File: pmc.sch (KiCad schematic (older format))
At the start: 165 parts, among them M1 TPS61040, M2 LM46001, M3 STM32F405RG, M4 REF3033, M5 TPS73633, M6 SN65HVD233, M7 UCC27211A, M8 UCC27211A, M9 UCC27211A, P1 FAN, P10 F1, P11 F2, P12 A1, P13 A2, P14 BOOT, P15 F1, P16 F2, P17 A1, P18 A2, P19 CONN4, P2 NTC, P20 CONN4, P21 CONN4, P22 CONN4, P23 CONN4, P3 HALL, P4 SPI, P5 PPM, P6 ANALOG, P7 CAN, P8 SWD, P9 USART, Q1 IRLML6401, Q2 IPT007N06N, Q3 IPT007N06N, Q4 IPT007N06N, Q5 IPT007N06N, Q6 IPT007N06N, Q7 IPT007N06N, U1 AD8539, U2 AD8539, U3 AD8417, U4 AD8417

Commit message: Moved CAN to 5v, fixed filter capacitors, etc.
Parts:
- removed M6: SN65HVD233, foot:SO-8, symbol SN65HVD23X
- removed R45, R46: 1K 1%, foot:SM-0603, symbol R
- added C66: 100nF 25v, foot:SM-0603, symbol C
- added M6: SN65HVD256, foot:SO-8, symbol SN65HVD256
- C41, C42, C43, C44: value 47pF C0G -> 1nF C0G
- R8: value 11.3K 1% -> 13.7K 1%
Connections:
- net +3.3V: now also C66.1, M6.5 (VRXD); no longer C35.2, C36.2
- net +5V: now also C35.2, C36.2, M6.3 (VCC)
- net AGND: now also C66.2, M6.2 (GND), M6.8 (S)
- net CAN_RX: now also M6.4 (RXD)
- net CAN_TX: now also M6.1 (TXD)
- net CURRENT_A: now also P17.3
- net CURRENT_B: now also P17.4
- net at P7.2, R35.1, R51.1: now also M6.6 (CANL)
- net at P7.1, R35.2, R51.2: now also M6.7 (CANH)
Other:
- note added: "Pulse control inputs:\n * RC servo pulse width\n * STEP/DIR\n * QEP\nor I2C bus or Data-USART"
- note added: "R33 is not fitted\n"
- note added: "Vfb = 1.016v"
- note added: "Vfb = 1.233v"
- note removed: "Balance resistors R45-R46 are needed only in case of parallel\nconnection of multiple power boards\n"
- note removed: "Pulse control inputs:\n * RC servo PPM\n * STEP/DIR\n * QEP\nor I2C bus or USART"
- note removed: "R33 is not fitted if 3.3vREF voltage reference is used\n"
- moved on the sheet: R35, R51
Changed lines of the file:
@@
 Sheet 1 1
 Title "Phobia Motor Controller"
-Date "2018-12-10"
+Date "2019-03-23"
 Rev "4c"
 Comp "Roman Belov"
@@
 P 5450 5250
 F 0 "R8" V 5550 5050 60  0000 C CNN
-F 1 "11.3K 1%" V 5400 4900 60  0000 C CNN
+F 1 "13.7K 1%" V 5400 4900 60  0000 C CNN
 F 2 "foot:SM-0603" H 5450 5250 60  0001 C CNN
 F 3 "" H 5450 5250 60  0000 C CNN
@@
 U 1 1 59D934A0
 P 13250 2050
-F 0 "C41" V 13350 1850 60  0000 C CNN
-F 1 "47pF C0G" V 13150 1700 60  0000 C CNN
+F 0 "C41" V 13300 1800 60  0000 C CNN
+F 1 "1nF C0G" V 13150 1700 60  0000 C CNN
 F 2 "foot:SM-0603" H 13250 2050 60  0001 C CNN
 F 3 "" H 13250 2050 60  0000 C CNN
@@
 	0    -1   -1   0
 $EndComp
-$Comp
-L SN65HVD23X M6
-U 1 1 59D934A6
-P 10050 13250
-F 0 "M6" H 10050 13600 60  0000 C CNN
-F 1 "SN65HVD233" H 10000 12900 60  0000 C CNN
-F 2 "foot:SO-8" H 9600 12900 60  0001 C CNN
-F 3 "" H 10050 13250 60  0000 C CNN
-	1    10050 13250
-	1    0    0    -1
-$EndComp
 Text GLabel 6850 9750 2    60   Input ~ 0
 CAN_RX
@@
 L +3.3V #PWR021
 U 1 1 59D934A7
-P 8900 14200
-F 0 "#PWR021" H 8900 14290 20  0001 C CNN
-F 1 "+3.3V" V 8900 14550 60  0000 C CNN
-F 2 "" H 8900 14200 60  0000 C CNN
-F 3 "" H 8900 14200 60  0000 C CNN
-	1    8900 14200
+P 10250 13750
+F 0 "#PWR021" H 10250 13840 20  0001 C CNN
+F 1 "+3.3V" V 10250 14100 60  0000 C CNN
+F 2 "" H 10250 13750 60  0000 C CNN
+F 3 "" H 10250 13750 60  0000 C CNN
+	1    10250 13750
 	0    -1   -1   0
 $EndComp
@@
 L R R35
 U 1 1 59D934AA
-P 11350 13400
-F 0 "R35" H 11750 13400 60  0000 C CNN
-F 1 "820" H 11000 13400 60  0000 C CNN
-F 2 "foot:SM-1206" H 11350 13400 60  0001 C CNN
-F 3 "" H 11350 13400 60  0000 C CNN
-	1    11350 13400
+P 11600 13400
+F 0 "R35" H 12000 13400 60  0000 C CNN
+F 1 "820" H 11250 13400 60  0000 C CNN
+F 2 "foot:SM-1206" H 11600 13400 60  0001 C CNN
+F 3 "" H 11600 13400 60  0000 C CNN
+	1    11600 13400
 	-1   0    0    1
 $EndComp
@@
 U 1 1 59D934AB
 P 9350 13750
-F 0 "C35" H 9000 13850 60  0000 C CNN
-F 1 "100nF 25v" H 9850 13650 60  0000 C CNN
+F 0 "C35" H 8950 13800 60  0000 C CNN
+F 1 "100nF 25v" H 8850 13650 60  0000 C CNN
 F 2 "foot:SM-0603" H 9350 13750 60  0001 C CNN
 F 3 "" H 9350 13750 60  0000 C CNN
@@
 U 1 1 59D934AC
 P 9350 14200
-F 0 "C36" H 9365 14030 60  0000 C CNN
-F 1 "1uF 25v" H 9800 14100 60  0000 C CNN
+F 0 "C36" H 9150 14050 60  0000 C CNN
+F 1 "1uF 25v" H 9200 13900 60  0000 C CNN
 F 2 "foot:SM-0805" H 9350 14200 60  0001 C CNN
 F 3 "" H 9350 14200 60  0000 C CNN
@@
 L GND #PWR023
 U 1 1 59D934AD
-P 10600 13850
-F 0 "#PWR023" H 10600 13850 30  0001 C CNN
-F 1 "GND" H 10600 13780 30  0001 C CNN
-F 2 "" H 10600 13850 60  0000 C CNN
-F 3 "" H 10600 13850 60  0000 C CNN
-	1    10600 13850
+P 10900 14150
+F 0 "#PWR023" H 10900 14150 30  0001 C CNN
+F 1 "GND" H 10900 14080 30  0001 C CNN
+F 2 "" H 10900 14150 60  0000 C CNN
+F 3 "" H 10900 14150 60  0000 C CNN
+	1    10900 14150
 	1    0    0    -1
 $EndComp
@@
 U 1 1 59D934C4
 P 13250 3400
-F 0 "C42" V 13350 3200 60  0000 C CNN
-F 1 "47pF C0G" V 13150 3050 60  0000 C CNN
+F 0 "C42" V 13300 3150 60  0000 C CNN
+F 1 "1nF C0G" V 13150 3050 60  0000 C CNN
 F 2 "foot:SM-0603" H 13250 3400 60  0001 C CNN
 F 3 "" H 13250 3400 60  0000 C CNN
@@
 U 1 1 59F72F54
 P 13250 4750
-F 0 "C43" V 13350 4550 60  0000 C CNN
-F 1 "47pF C0G" V 13150 4400 60  0000 C CNN
+F 0 "C43" V 13300 4500 60  0000 C CNN
+F 1 "1nF C0G" V 13150 4400 60  0000 C CNN
 F 2 "foot:SM-0603" H 13250 4750 60  0001 C CNN
 F 3 "" H 13250 4750 60  0000 C CNN
@@
 U 1 1 59F72F7F
 P 13250 6100
-F 0 "C44" V 13350 5900 60  0000 C CNN
-F 1 "47pF C0G" V 13150 5750 60  0000 C CNN
+F 0 "C44" V 13300 5850 60  0000 C CNN
+F 1 "1nF C0G" V 13150 5750 60  0000 C CNN
 F 2 "foot:SM-0603" H 13250 6100 60  0001 C CNN
 F 3 "" H 13250 6100 60  0000 C CNN
@@
 External peripheral SPI device\nor ADC/DAC or GPIO
 Text Notes 12600 10600 0    60   ~ 0
-Pulse control inputs:\n * RC servo PPM\n * STEP/DIR\n * QEP\nor I2C bus or USART
+Pulse control inputs:\n * RC servo pulse width\n * STEP/DIR\n * QEP\nor I2C bus or Data-USART
 Text Notes 15100 14150 0    60   ~ 0
 Flash STM32 microcontroller\nDebug via SWD\nConfigure and control via USART\n
@@
 ADC_IN11
 $Comp
-L R R46
-U 1 1 5B00BFA8
-P 18850 10400
-F 0 "R46" H 19050 10550 60  0000 C CNN
-F 1 "1K 1%" H 18750 10550 60  0000 C CNN
-F 2 "foot:SM-0603" H 18850 10400 60  0001 C CNN
-F 3 "" H 18850 10400 60  0000 C CNN
-	1    18850 10400
-	1    0    0    -1
-$EndComp
-$Comp
-L R R45
-U 1 1 5B0107B7
-P 18350 10500
-F 0 "R45" H 18550 10350 60  0000 C CNN
-F 1 "1K 1%" H 18250 10350 60  0000 C CNN
-F 2 "foot:SM-0603" H 18350 10500 60  0001 C CNN
-F 3 "" H 18350 10500 60  0000 C CNN
-	1    18350 10500
-	1    0    0    -1
-$EndComp
-$Comp
 L R R33
 U 1 1 5B5F338A
@@
 	0    -1   -1   0
 $EndComp
-Text Notes 10700 12900 0    60   ~ 12
+Text Notes 11150 13900 0    60   ~ 12
 Optional termination resistors
 $Comp
@@
 L R R51
 U 1 1 5C351474
-P 11350 13600
-F 0 "R51" H 11750 13600 60  0000 C CNN
-F 1 "820" H 11000 13600 60  0000 C CNN
-F 2 "foot:SM-1206" H 11350 13600 60  0001 C CNN
-F 3 "" H 11350 13600 60  0000 C CNN
-	1    11350 13600
+P 11600 13600
+F 0 "R51" H 12000 13600 60  0000 C CNN
+F 1 "820" H 11250 13600 60  0000 C CNN
+F 2 "foot:SM-1206" H 11600 13600 60  0001 C CNN
+F 3 "" H 11600 13600 60  0000 C CNN
+	1    11600 13600
+	-1   0    0    1
+$EndComp
+Text Notes 18650 12650 0    60   ~ 12
+Current sensing range\n\nRange (A)   Shunt (mOhm)\n-----------------\n      50       0.5\n      80       0.3\n     100      0.25
+Text Notes 10500 3550 0    60   ~ 12
+R33 is not fitted\n
+Text Notes 5550 1750 0    60   ~ 12
+Vfb = 1.016v
+Text Notes 5100 4450 0    60   ~ 12
+Vfb = 1.233v
+$Comp
+L +5V #PWR0107
+U 1 1 5C89DA1F
+P 8900 14200
+F 0 "#PWR0107" H 8900 14290 20  0001 C CNN
+F 1 "+5V" V 8900 14500 60  0000 C CNN
+F 2 "" H 8900 14200 60  0000 C CNN
+F 3 "" H 8900 14200 60  0000 C CNN
+	1    8900 14200
+	0    -1   -1   0
+$EndComp
+$Comp
+L SN65HVD256 M6
+U 1 1 5C8A5FB5
+P 10050 13250
+F 0 "M6" H 9800 13600 60  0000 C CNN
+F 1 "SN65HVD256" H 10250 13600 60  0000 C CNN
+F 2 "foot:SO-8" H 9600 12900 60  0001 C CNN
+F 3 "" H 10050 13250 60  0000 C CNN
+	1    10050 13250
+	1    0    0    -1
+$EndComp
+$Comp
+L C C66
+U 1 1 5C8AE35E
+P 10700 13750
+F 0 "C66" H 10900 13900 60  0000 C CNN
+F 1 "100nF 25v" H 10850 14050 60  0000 C CNN
+F 2 "foot:SM-0603" H 10700 13750 60  0001 C CNN
+F 3 "" H 10700 13750 60  0000 C CNN
+	1    10700 13750
 	-1   0    0    1
 $EndComp
@@
 Wire Wire Line
 	6700 11500 6700 11600
-Connection ~ 10600 13400
-Wire Wire Line
-	10500 13400 10600 13400
-Wire Wire Line
-	10600 13300 10500 13300
-Wire Wire Line
-	10600 13300 10600 13850
-Connection ~ 11500 13100
-Connection ~ 11150 13200
+Connection ~ 11750 13100
+Connection ~ 11400 13200
 Wire Wire Line
 	10500 13200 12000 13200
@@
 	16300 10200 16100 10200
 Wire Wire Line
-	17400 10400 18700 10400
-Wire Wire Line
 	18500 11300 17400 11300
 Wire Wire Line
@@
 	15200 10400 16300 10400
 Wire Wire Line
-	19050 10400 19300 10400
-Wire Wire Line
-	17400 10500 18200 10500
-Wire Wire Line
-	18550 10500 18700 10500
-Wire Wire Line
 	18700 10500 18700 10600
 Wire Wire Line
@@
 Connection ~ 8650 4700
 Wire Wire Line
-	11150 13200 11150 13600
-Connection ~ 11150 13400
+	11400 13200 11400 13600
+Connection ~ 11400 13400
 Wire Wire Line
-	11500 13100 11500 13600
-Connection ~ 11500 13400
-Text Notes 18650 12650 0    60   ~ 12
-Current sensing range\n\nRange (A)   Shunt (mOhm)\n-----------------\n      50       0.5\n      80       0.3\n     100      0.25
-Text Notes 18750 10950 0    60   ~ 12
-Balance resistors R45-R46 are needed only in case of parallel\nconnection of multiple power boards\n
-Text Notes 9250 4000 0    60   ~ 12
-R33 is not fitted if 3.3vREF voltage reference is used\n
+	11750 13100 11750 13600
+Connection ~ 11750 13400
+Wire Wire Line
+	10500 13300 10900 13300
+Wire Wire Line
+	10900 13750 10850 13750
+Wire Wire Line
+	10250 13750 10550 13750
+Connection ~ 10500 13750
+Connection ~ 10900 13750
+Wire Wire Line
+	10500 13750 10500 13400
+Wire Wire Line
+	10900 13300 10900 14150
+Wire Wire Line
+	18700 10500 17400 10500
+Wire Wire Line
+	17400 10400 19300 10400
 $EndSCHEMATC

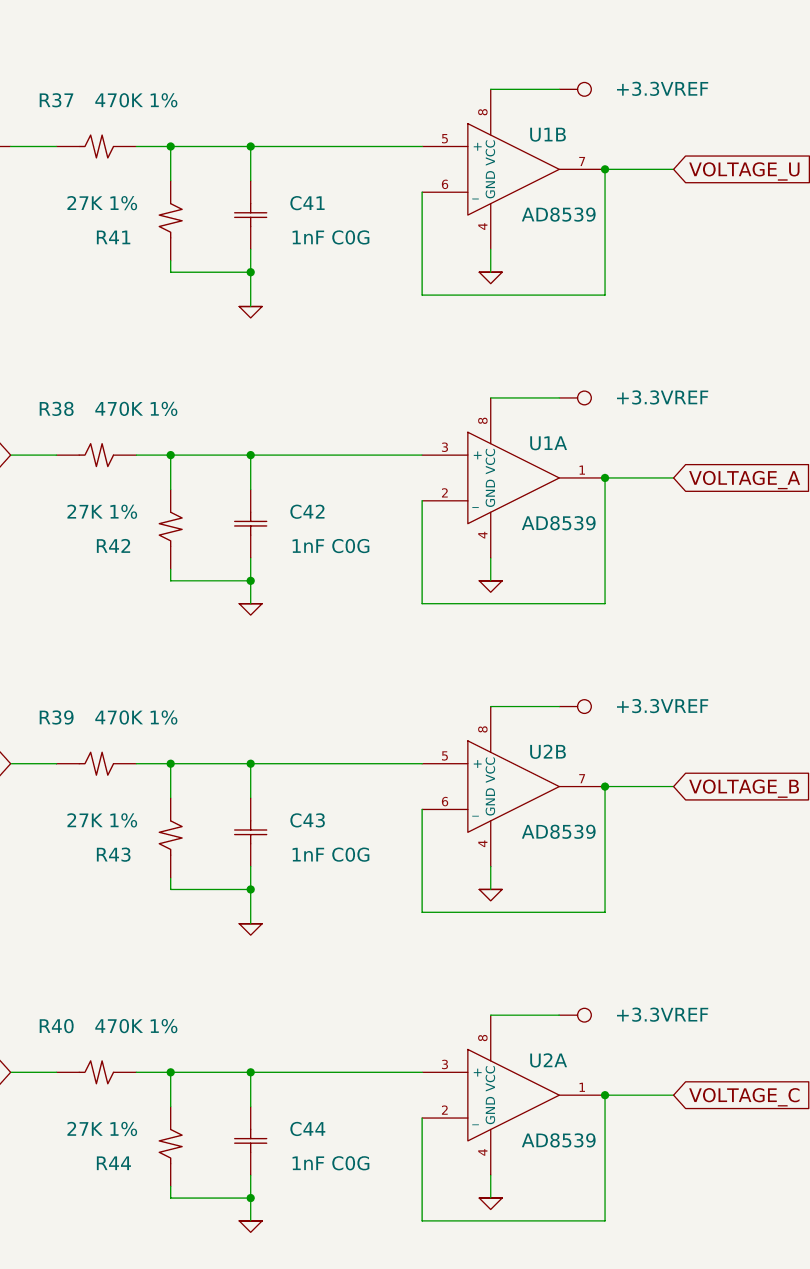
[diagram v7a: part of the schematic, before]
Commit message: Added voltage bias resistors.
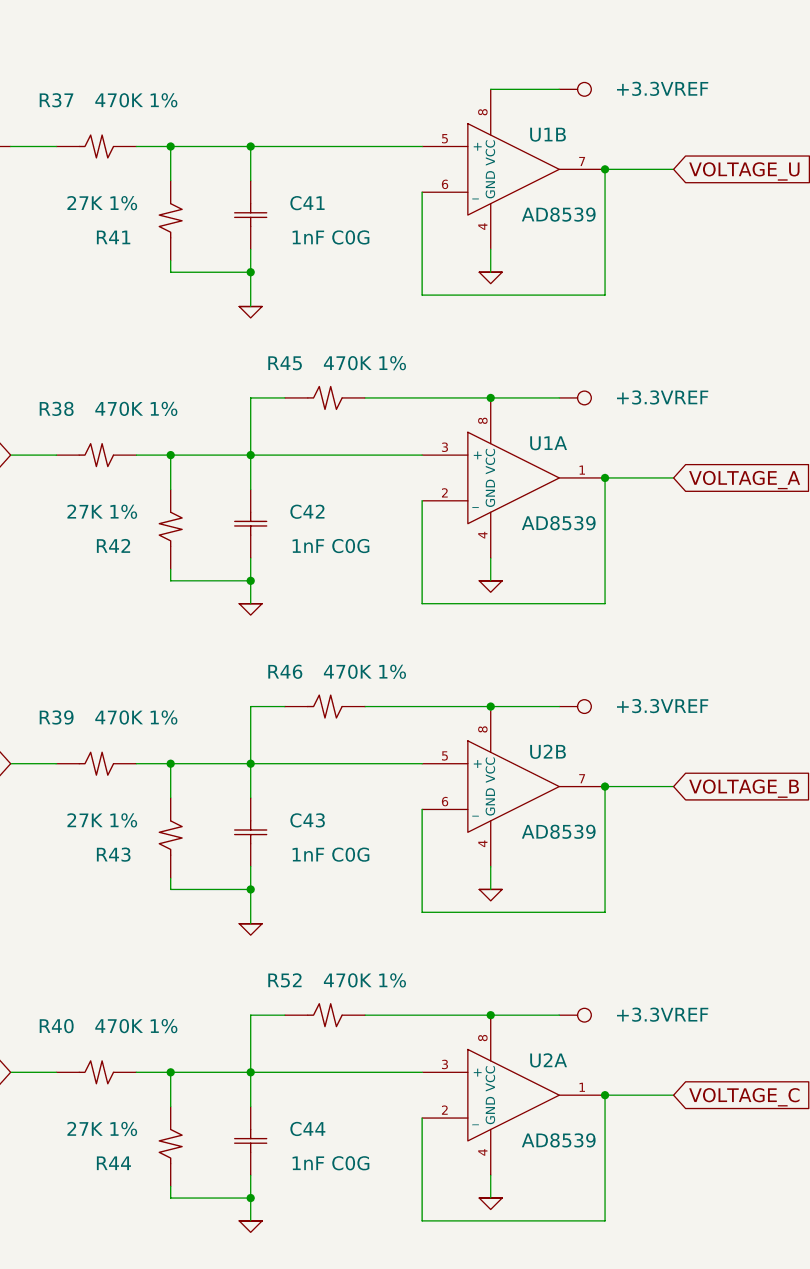
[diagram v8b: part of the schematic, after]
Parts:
- added R45, R46, R52: 470K 1%, foot:SM-0603, symbol R
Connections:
- net +3.3VREF: now also R45.2, R46.2, R52.2
- net at C42.1, R38.2, R42.2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: now also R45.1
- net at C43.1, R39.2, R43.2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: now also R46.1
- net at C44.1, R40.2, R44.2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: now also R52.1
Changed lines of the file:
@@
 Sheet 1 1
 Title "Phobia Motor Controller"
-Date "2019-03-23"
+Date "2019-04-27"
 Rev "4c"
 Comp "Roman Belov"
@@
 	13250 3550 13250 3750
 Wire Wire Line
-	13250 3100 13250 3250
+	13250 2850 13250 3250
 Wire Wire Line
 	13250 2200 13250 2450
 Wire Wire Line
-	13250 1750 13250 1900
-Wire Wire Line
-	14600 2850 14300 2850
-Wire Wire Line
-	14300 1500 14600 1500
+	13750 2850 14600 2850
 Wire Wire Line
 	14300 3550 14300 3650
@@
 	13250 6250 13250 6450
 Wire Wire Line
-	13250 5800 13250 5950
+	13250 5550 13250 5950
 Wire Wire Line
 	13250 4900 13250 5150
 Wire Wire Line
-	13250 4450 13250 4600
+	13250 4200 13250 4600
 Wire Wire Line
-	14600 5550 14300 5550
+	13750 5550 14600 5550
 Wire Wire Line
-	14300 4200 14600 4200
+	13750 4200 14600 4200
 Wire Wire Line
 	14300 6250 14300 6350
@@
 Wire Wire Line
 	17400 10400 19300 10400
+$Comp
+L R R45
+U 1 1 5CBCA564
+P 13600 2850
+F 0 "R45" H 13800 2700 60  0000 C CNN
+F 1 "470K 1%" H 13450 2700 60  0000 C CNN
+F 2 "foot:SM-0603" H 13600 2850 60  0001 C CNN
+F 3 "" H 13600 2850 60  0000 C CNN
+	1    13600 2850
+	-1   0    0    1
+$EndComp
+$Comp
+L R R46
+U 1 1 5CBCB0D2
+P 13600 4200
+F 0 "R46" H 13800 4050 60  0000 C CNN
+F 1 "470K 1%" H 13450 4050 60  0000 C CNN
+F 2 "foot:SM-0603" H 13600 4200 60  0001 C CNN
+F 3 "" H 13600 4200 60  0000 C CNN
+	1    13600 4200
+	-1   0    0    1
+$EndComp
+$Comp
+L R R52
+U 1 1 5CBCB5B7
+P 13600 5550
+F 0 "R52" H 13800 5400 60  0000 C CNN
+F 1 "470K 1%" H 13450 5400 60  0000 C CNN
+F 2 "foot:SM-0603" H 13600 5550 60  0001 C CNN
+F 3 "" H 13600 5550 60  0000 C CNN
+	1    13600 5550
+	-1   0    0    1
+$EndComp
+Wire Wire Line
+	14600 1500 14300 1500
+Wire Wire Line
+	13250 1900 13250 1750
+Wire Wire Line
+	13400 2850 13250 2850
+Connection ~ 14300 2850
+Wire Wire Line
+	13400 4200 13250 4200
+Connection ~ 14300 4200
+Wire Wire Line
+	13400 5550 13250 5550
+Connection ~ 14300 5550
 $EndSCHEMATC
